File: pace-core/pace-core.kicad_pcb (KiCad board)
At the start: 4 copper layers, 100 x 100 mm, 155 parts, among them CN1 XT90PW-M.G.Y, CN2 SMTSOM330BTR, CN3 SMTSOM330BTR, CN4 SMTSOM330BTR, CN5 SMTSOM330BTR, CN6 SMTSOM330BTR, CN7 SMTSOM330BTR, J1 MotorOut, J2 Wiz5500-Coprocessor-BoB, J3 Conn_01x05, J4 Conn_02x05_Odd_Even, J6 Conn_01x05, Q10 ISC0802NLSATMA1, Q11 ISC0802NLSATMA1, Q12 ISC0802NLSATMA1, Q7 ISC0802NLSATMA1, Q8 ISC0802NLSATMA1, Q9 ISC0802NLSATMA1, SW1 SKRPACE010, SW2 SKRPACE010, SW3 DPDT, U1 ESP32-S3-WROOM-1, U10 LM75ADP,118, U11 LM75ADP,118, U2 DRV8353SRTAT, U3 USBLC6-2P6, U4 ADUM3160BRWZ-RL, U5 AMS1117-3.3, U6 XL7015E1, U7 REF35160QDBVR, U8 LM75ADP,118, U9 LM75ADP,118

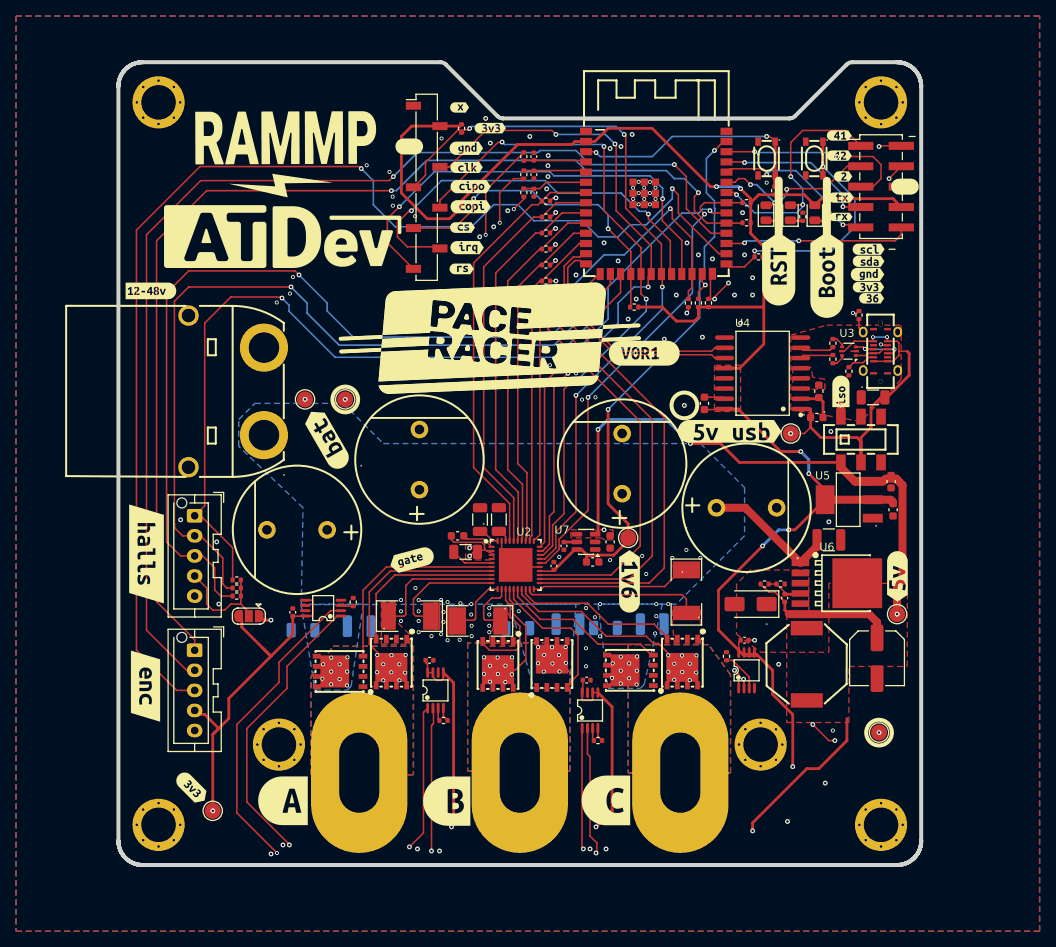
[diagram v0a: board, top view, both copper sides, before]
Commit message: design checkpoint: v1 repackage — new connectors, footprints, and layout updates
- Add JST SH/SR series, XT30PW-M, TH cap, and SOT-23-3 footprints with 3D models
- Update connectors, power-reg, and mechanicals schematic sheets
- Rework PCB layout and update board STEP exports (r0 updated, r2 added)
- Regenerate interactive BOM

Co-Authored-By: Claude Fable 5 <noreply@anthropic.com>
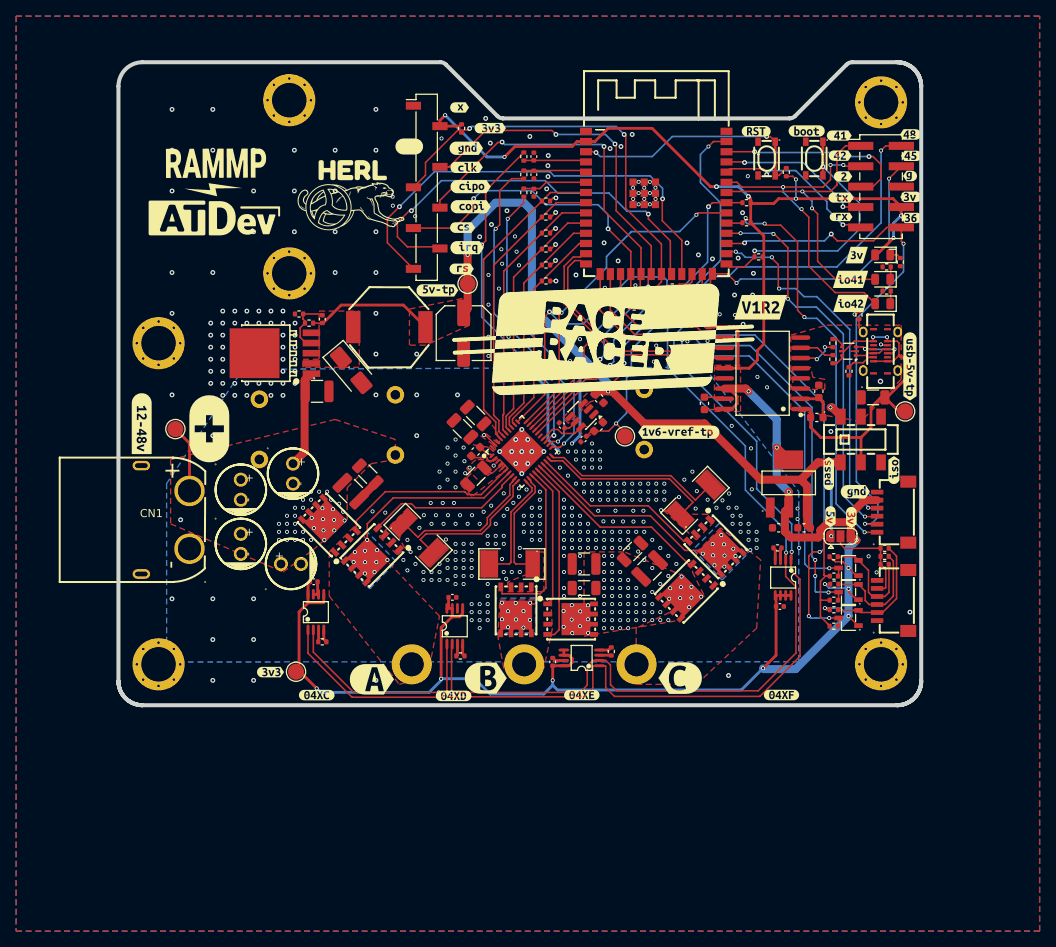
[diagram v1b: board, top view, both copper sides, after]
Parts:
- removed C22: 470uF 100V, specific-parts-lib:CAP-TH_BD16.0-P7.50-D1.2-FD
- removed J3, J6: Conn_01x05, Connector_JST:JST_XA_B05B-XASK-1-A_1x05_P2.50mm_Vertical
- removed TP26, TP27: TestPoint, TestPoint:TestPoint_Pad_D2.0mm
- removed kibuzzard-6A1922D9: G***, kibuzzard-6A1922D9
- removed kibuzzard-6A192300: G***, kibuzzard-6A192300
- removed kibuzzard-6A1923D8: G***, kibuzzard-6A1923D8
- removed kibuzzard-6A1923EE: G***, kibuzzard-6A1923EE
- removed kibuzzard-6A1923F4: G***, kibuzzard-6A1923F4
- removed kibuzzard-6A1924A7: G***, kibuzzard-6A1924A7
- removed kibuzzard-6A1924C5: G***, kibuzzard-6A1924C5
- removed kibuzzard-6A192600: G***, kibuzzard-6A192600
- removed kibuzzard-6A192643: G***, kibuzzard-6A192643
- removed kibuzzard-6A1926BF: G***, kibuzzard-6A1926BF
- removed kibuzzard-6A19287E: G***, kibuzzard-6A19287E
- removed kibuzzard-6A1928AF: G***, kibuzzard-6A1928AF
- removed kibuzzard-6A192988: G***, kibuzzard-6A192988
- removed kibuzzard-6A192993: G***, kibuzzard-6A192993
- removed kibuzzard-6A1929A7: G***, kibuzzard-6A1929A7
- removed kibuzzard-6A1929C1: G***, kibuzzard-6A1929C1
- removed kibuzzard-6A1929FE: G***, kibuzzard-6A1929FE
- removed kibuzzard-6A19324D: G***, kibuzzard-6A19324D
- removed kibuzzard-6A19331B: G***, kibuzzard-6A19331B
- removed kibuzzard-6A193462: G***, kibuzzard-6A193462
- removed kibuzzard-6A1936CE: G***, kibuzzard-6A1936CE
- removed kibuzzard-6A193793: G***, kibuzzard-6A193793
- removed kibuzzard-6A193F0C: G***, kibuzzard-6A193F0C
- added C36: PA100V22M6X9, specific-parts-lib:CAP-TH_BD6.3-P2.50-D0.6-FD, F.Cu at (121.8, 101.2)
- added C37: PA100V22M6X9, specific-parts-lib:CAP-TH_BD6.3-P2.50-D0.6-FD, F.Cu at (121.5, 112.5)
- added C38: PA100V22M6X9, specific-parts-lib:CAP-TH_BD6.3-P2.50-D0.6-FD, F.Cu at (115.2, 110.0)
- added C39: PA100V22M6X9, specific-parts-lib:CAP-TH_BD6.3-P2.50-D0.6-FD, F.Cu at (115.2, 103.2)
- added Q1: BSS138, specific-parts-lib:SOT-23-3_L2.9-W1.6-P1.90-LS2.8-BR, F.Cu at (190.9, 119.2)
- added Q2: BSS138, specific-parts-lib:SOT-23-3_L2.9-W1.6-P1.90-LS2.8-BR, F.Cu at (190.9, 116.0)
- added Q3: BSS138, specific-parts-lib:SOT-23-3_L2.9-W1.6-P1.90-LS2.8-BR, F.Cu at (190.9, 113.0)
- added R25: 10k, Resistor_SMD:R_0402_1005Metric, F.Cu at (189.1, 120.3)
- added R33: 10k, Resistor_SMD:R_0402_1005Metric, F.Cu at (189.1, 117.0)
- added R34: 10k, Resistor_SMD:R_0402_1005Metric, F.Cu at (189.1, 114.0)
- added R41: 10k, Resistor_SMD:R_0402_1005Metric, F.Cu at (189.1, 118.2)
- added R42: 10k, Resistor_SMD:R_0402_1005Metric, F.Cu at (189.2, 115.0)
- added R43: 10k, Resistor_SMD:R_0402_1005Metric, F.Cu at (189.1, 111.6)
- added U12: SM06B-SRSS-TB, specific-parts-lib:CONN-SMD_SM06B-SRSS-TB-LF-SN, F.Cu at (196.4, 106.0)
- added U13: SM06B-SRSS-TB, specific-parts-lib:CONN-SMD_SM06B-SRSS-TB-LF-SN, F.Cu at (196.4, 117.0)
- added kibuzzard-6A769215: G***, kibuzzard-6A769215, F.Cu at (102.9, 95.0)
- added kibuzzard-6A76A548: G***, kibuzzard-6A76A548, F.Cu at (180.0, 80.5)
- added kibuzzard-6A76A5A9: G***, kibuzzard-6A76A5A9, F.Cu at (192.0, 74.0)
- added kibuzzard-6A76A5E2: G***, kibuzzard-6A76A5E2, F.Cu at (191.2, 77.0)
- added kibuzzard-6A76A5F0: G***, kibuzzard-6A76A5F0, F.Cu at (191.2, 80.0)
- added kibuzzard-6A76A71C: G***, kibuzzard-6A76A71C, F.Cu at (129.2, 63.5)
- added kibuzzard-6A76A790: G***, kibuzzard-6A76A790, F.Cu at (111.3, 95.7)
- added kibuzzard-6A76A7BD: G***, kibuzzard-6A76A7BD, F.Cu at (179.4, 58.6)
- added kibuzzard-6A76A7CE: G***, kibuzzard-6A76A7CE, F.Cu at (185.7, 58.6)
- added kibuzzard-6A76A802: G***, kibuzzard-6A76A802, F.Cu at (189.9, 61.6)
- added kibuzzard-6A76A80F: G***, kibuzzard-6A76A80F, F.Cu at (189.8, 59.1)
- added kibuzzard-6A76A83C: G***, kibuzzard-6A76A83C, F.Cu at (198.7, 66.8)
- added kibuzzard-6A76A86B: G***, kibuzzard-6A76A86B, F.Cu at (198.6, 64.2)
- added kibuzzard-6A76A8BC: G***, kibuzzard-6A76A8BC, F.Cu at (198.8, 69.4)
- added kibuzzard-6A76A904: G***, kibuzzard-6A76A904, F.Cu at (198.7, 59.0)
- added kibuzzard-6A76A908: G***, kibuzzard-6A76A908, F.Cu at (198.8, 61.7)
- added kibuzzard-6A76A991: G***, kibuzzard-6A76A991, F.Cu at (196.6, 100.8)
- added kibuzzard-6A76A9E7: G***, kibuzzard-6A76A9E7, F.Cu at (188.5, 101.2)
- added kibuzzard-6A76AA0A: G***, kibuzzard-6A76AA0A, F.Cu at (198.6, 87.9)
- added kibuzzard-6A76AA3B: G***, kibuzzard-6A76AA3B, F.Cu at (169.8, 96.1)
- added kibuzzard-6A76AAA5: G***, kibuzzard-6A76AAA5, F.Cu at (145.8, 126.7)
- added kibuzzard-6A76AAC0: G***, kibuzzard-6A76AAC0, F.Cu at (131.6, 126.9)
- added kibuzzard-6A76AAE1: G***, kibuzzard-6A76AAE1, F.Cu at (170.0, 126.7)
- added kibuzzard-6A76AB0C: G***, kibuzzard-6A76AB0C, F.Cu at (124.7, 128.8)
- added kibuzzard-6A76AB7D: G***, kibuzzard-6A76AB7D, F.Cu at (141.8, 128.9)
- added kibuzzard-6A76AB8B: G***, kibuzzard-6A76AB8B, F.Cu at (157.7, 128.8)
- added kibuzzard-6A76AB97: G***, kibuzzard-6A76AB97, F.Cu at (182.6, 128.8)
- added kibuzzard-6A76ABC4: G***, kibuzzard-6A76ABC4, F.Cu at (139.7, 78.4)
- added kibuzzard-6A76AD5A: G***, kibuzzard-6A76AD5A, F.Cu at (188.7, 106.6)
- added kibuzzard-6A76AD71: G***, kibuzzard-6A76AD71, F.Cu at (191.3, 106.7)
- added kibuzzard-6A76AD7E: G***, kibuzzard-6A76AD7E, F.Cu at (191.8, 103.5)
- added kibuzzard-6A793D41: G***, kibuzzard-6A793D41, F.Cu at (118.9, 126.0)
- C11, C12, C13, C6, C7, C8: moved to F.Cu
- C19, C20, C21: moved to B.Cu
- CN1: value XT90PW-M.G.Y -> XT60PW-M; footprint specific-parts-lib:CONN-TH_XT90PW-M.G.Y -> specific-parts-lib:CONN-TH_XT60PW-M
- moved CN6 99.5 mm to (121.3, 54.7)
- moved R18 80.8 mm to (195.4, 110.5), turned to 180 degrees
- moved R19 80.8 mm to (195.4, 111.5), turned to 180 degrees
- moved R20 80.8 mm to (195.4, 112.5), turned to 180 degrees
- moved JP4 74.4 mm to (189.9, 109.0), turned to 0 degrees
- moved U6 73.8 mm to (120.5, 86.2), turned to 180 degrees
- moved R15 68.8 mm to (122.5, 81.4), turned to 180 degrees
- moved TP19 67.5 mm to (143.5, 77.6)
- moved C16 67.3 mm to (125.4, 82.0)
- moved L2 66.8 mm to (133.8, 83.0), turned to 0 degrees
- moved C35 66.4 mm to (124.8, 91.0)
- moved C17 65.5 mm to (143.0, 83.8)
- moved R14 65.4 mm to (123.8, 82.5), turned to 180 degrees
- moved C20 61.5 mm to (117.6, 95.7), turned to 90 degrees
- moved CN7 58.7 mm to (121.3, 76.3)
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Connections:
- net GPIO36 renamed enc-spi-copi
- net Net-(J6-Pin_4) renamed /Connectors/v_pullup
- CN1 pad 1: +BATT -> GND
- CN1 pad 2: GND -> +BATT
- R18 pad 1: C-Halls -> Net-(Q1-S)
- R19 pad 1: B-Halls -> Net-(Q2-S)
- R20 pad 1: A-halls -> Net-(Q3-S)
- R6 pad 1: Net-(U4-UD–) -> Net-(U4-UD+)
- R7 pad 1: Net-(U4-UD+) -> Net-(U4-UD–)
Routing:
- net enc-spi-cipo: track 154.0 -> 45.5 mm, vias 2 -> 4
- net i2c-SCL: track 273.2 -> 180.1 mm, vias 8 -> 5
- net enc-spi-clk: track 140.5 -> 49.0 mm, vias 2 -> 4
- net i2c-SDA: track 258.4 -> 172.8 mm, vias 7 -> 4
- net enc-spi-cs: track 135.4 -> 52.8 mm, vias 2 -> 4
- net +5V: track 211.2 -> 129.3 mm, vias 6 -> 4
- net +3V3: track 383.0 -> 332.5 mm, vias 10 -> 21
- net A-halls: track 107.1 -> 60.0 mm
- net enc-spi-copi: track 23.1 -> 66.6 mm, vias 2 -> 4
- net B-Halls: track 104.0 -> 61.7 mm, vias 2 -> 4
- net Net-(U2-SOC): track 71.1 -> 37.3 mm
- net Net-(U2-SOB): track 72.3 -> 40.4 mm
- net Net-(U2-SOA): track 73.6 -> 42.5 mm
- net C-Halls: track 97.3 -> 67.3 mm, vias 2 -> 4
- net /MC-enable: track 63.7 -> 39.5 mm
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- added copper zone on F.Cu, net /Gate Driver and Half Bridges/src-NA
- added copper zone on F.Cu, net /Gate Driver and Half Bridges/src-NB
- added copper zone on F.Cu, net /Gate Driver and Half Bridges/src-NC
- added copper zone on F.Cu, net 1V6-REF
- added copper zone on F.Cu, net Net-(U2-DVDD)
- added copper zone on F.Cu, net Net-(U2-VCP)
- added copper zone on F.Cu, net Net-(U2-VGLS)
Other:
- board size 100 x 100 mm -> 100 x 80.1 mm
